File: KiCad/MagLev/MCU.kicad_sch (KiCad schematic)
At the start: 73 parts, among them J2 Programming header, J4 USB_B_Micro, Q1 ZX5T851GTA, Q16 TEMT7000X01, U6 ATmega328P-A, U8 FT232RL, U9 LM1117MP-5.0, Y3 J49SMH-16MHz

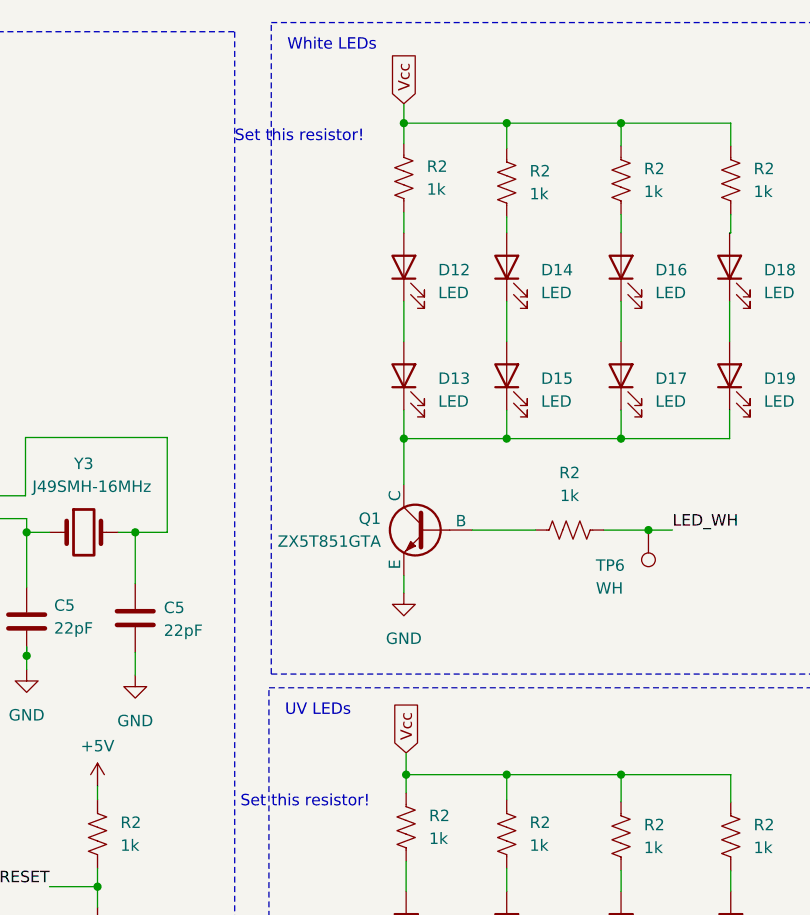
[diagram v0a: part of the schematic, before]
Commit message: Finish layout up to TPs.
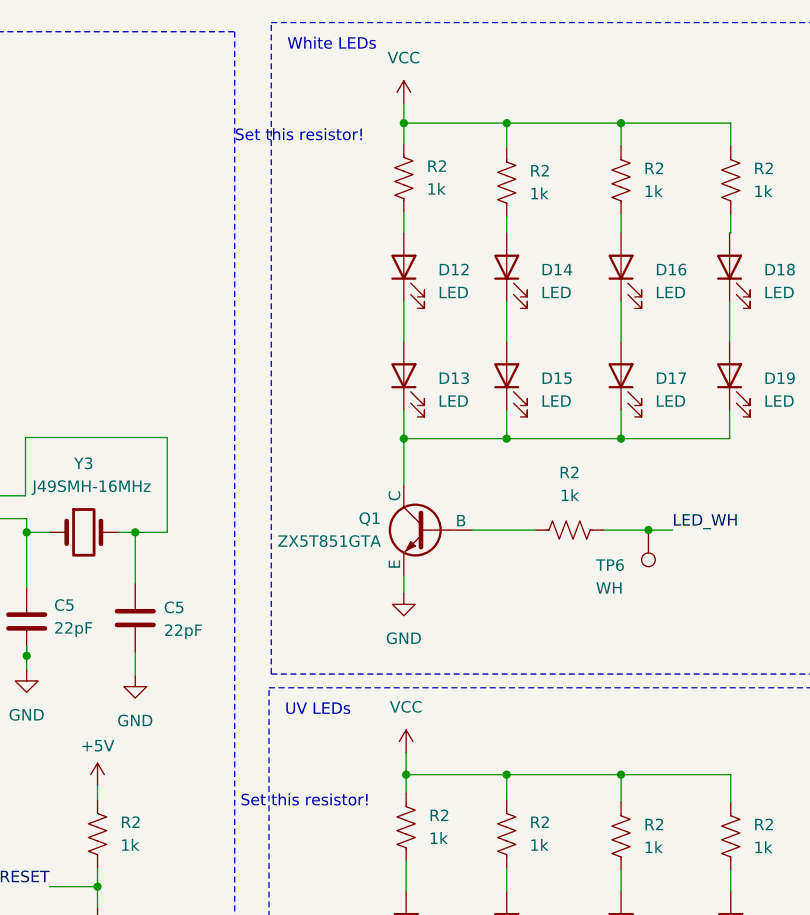
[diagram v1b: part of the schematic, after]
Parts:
- J4: footprint Connector_USB:USB_Micro-B_Amphenol_10118193-0001LF_Horizontal -> Connector_USB:USB_Micro-B_Amphenol_10104110_Horizontal
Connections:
- net Vcc is gone; now on net VCC: R2.2, R2.2, R2.2, R2.2, R2.2, R2.2, R2.2, R2.2
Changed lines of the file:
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@@
     (effects (font (size 1.27 1.27)) (justify left bottom))
-  )
-  (global_label "Vcc" (shape input) (at 235.458 25.527 90) (fields_autoplaced)
-    (effects (font (size 1.27 1.27)) (justify left))
-    (property "Intersheetrefs" "${INTERSHEET_REFS}" (at 235.458 19.276 90)
-      (effects (font (size 1.27 1.27)) (justify left) hide)
-    )
-  )
-  (global_label "Vcc" (shape input) (at 235.712 97.663 90) (fields_autoplaced)
-    (effects (font (size 1.27 1.27)) (justify left))
-    (property "Intersheetrefs" "${INTERSHEET_REFS}" (at 235.712 91.412 90)
-      (effects (font (size 1.27 1.27)) (justify left) hide)
-    )
   )
   (hierarchical_label "En_sig" (shape input) (at 178.816 102.108 0) (fields_autoplaced)
@@
     )
   )
+  (symbol (lib_id "power:VCC") (at 235.458 25.527 0) (unit 1)
+    (in_bom yes) (on_board yes) (dnp no) (fields_autoplaced)
+    (property "Reference" "#PWR048" (at 235.458 29.337 0)
+      (effects (font (size 1.27 1.27)) hide)
+    )
+    (property "Value" "VCC" (at 235.458 20.447 0)
+      (effects (font (size 1.27 1.27)))
+    )
+    (property "Footprint" "" (at 235.458 25.527 0)
+      (effects (font (size 1.27 1.27)) hide)
+    )
+    (property "Datasheet" "" (at 235.458 25.527 0)
+      (effects (font (size 1.27 1.27)) hide)
+    )
+    (pin "1")
+    (instances
+      (project "MagLev"
+        (path "/5eab7e8b-54e1-47d0-9dc3-1e7c3fa2f560"
+          (reference "#PWR048") (unit 1)
+        )
+        (path "/5eab7e8b-54e1-47d0-9dc3-1e7c3fa2f560/f228425d-6c39-40c9-8e00-a9ebad8217db"
+          (reference "#PWR048") (unit 1)
+        )
+      )
+    )
+  )
   (symbol (lib_id "Device:LED") (at 235.458 55.753 90) (unit 1)
     (in_bom yes) (on_board yes) (dnp no) (fields_autoplaced)
@@
       (effects (font (size 1.27 1.27)))
     )
-    (property "Footprint" "Connector_USB:USB_Micro-B_Amphenol_10118193-0001LF_Horizontal" (at 33.147 85.598 0)
+    (property "Footprint" "Connector_USB:USB_Micro-B_Amphenol_10104110_Horizontal" (at 33.147 85.598 0)
       (effects (font (size 1.27 1.27)) hide)
     )
@@
         )
       )
+    )
+  )
+  (symbol (lib_id "power:VCC") (at 235.712 97.663 0) (unit 1)
+    (in_bom yes) (on_board yes) (dnp no) (fields_autoplaced)
+    (property "Reference" "#PWR048" (at 235.712 101.473 0)
+      (effects (font (size 1.27 1.27)) hide)
+    )
+    (property "Value" "VCC" (at 235.712 92.583 0)
+      (effects (font (size 1.27 1.27)))
+    )
+    (property "Footprint" "" (at 235.712 97.663 0)
+      (effects (font (size 1.27 1.27)) hide)
+    )
+    (property "Datasheet" "" (at 235.712 97.663 0)
+      (effects (font (size 1.27 1.27)) hide)
+    )
+    (pin "1")
+    (instances
+      (project "MagLev"
+        (path "/5eab7e8b-54e1-47d0-9dc3-1e7c3fa2f560"
+          (reference "#PWR048") (unit 1)
+        )
+        (path "/5eab7e8b-54e1-47d0-9dc3-1e7c3fa2f560/f228425d-6c39-40c9-8e00-a9ebad8217db"
+          (reference "#PWR053") (unit 1)
+        )
+      )

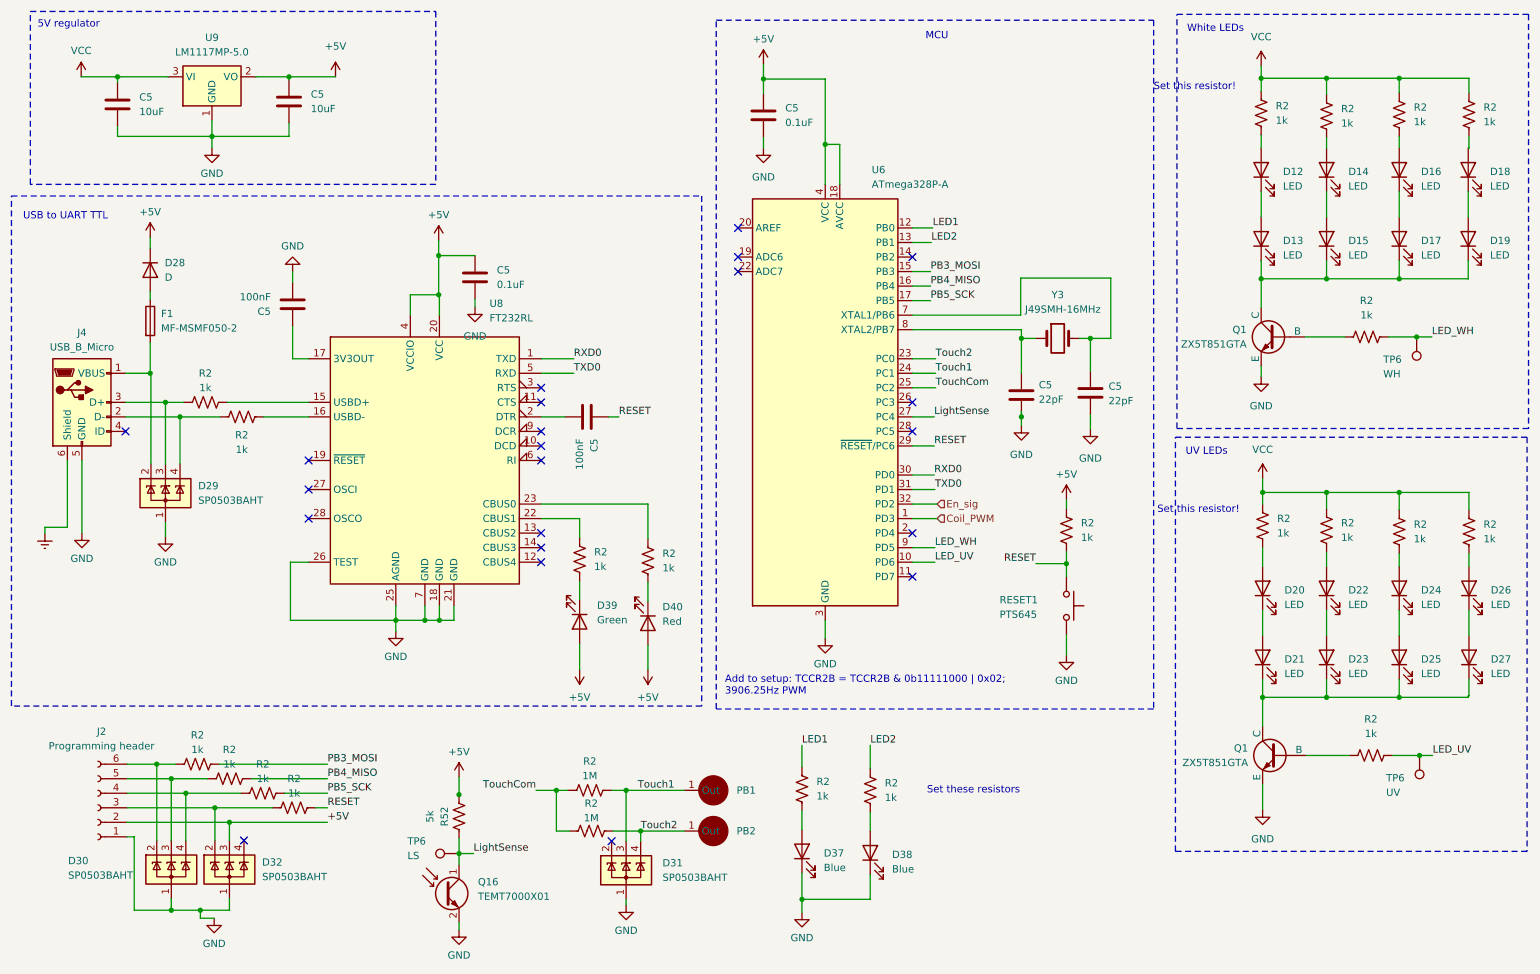
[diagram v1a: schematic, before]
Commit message: Route TPs, increase power trace size.
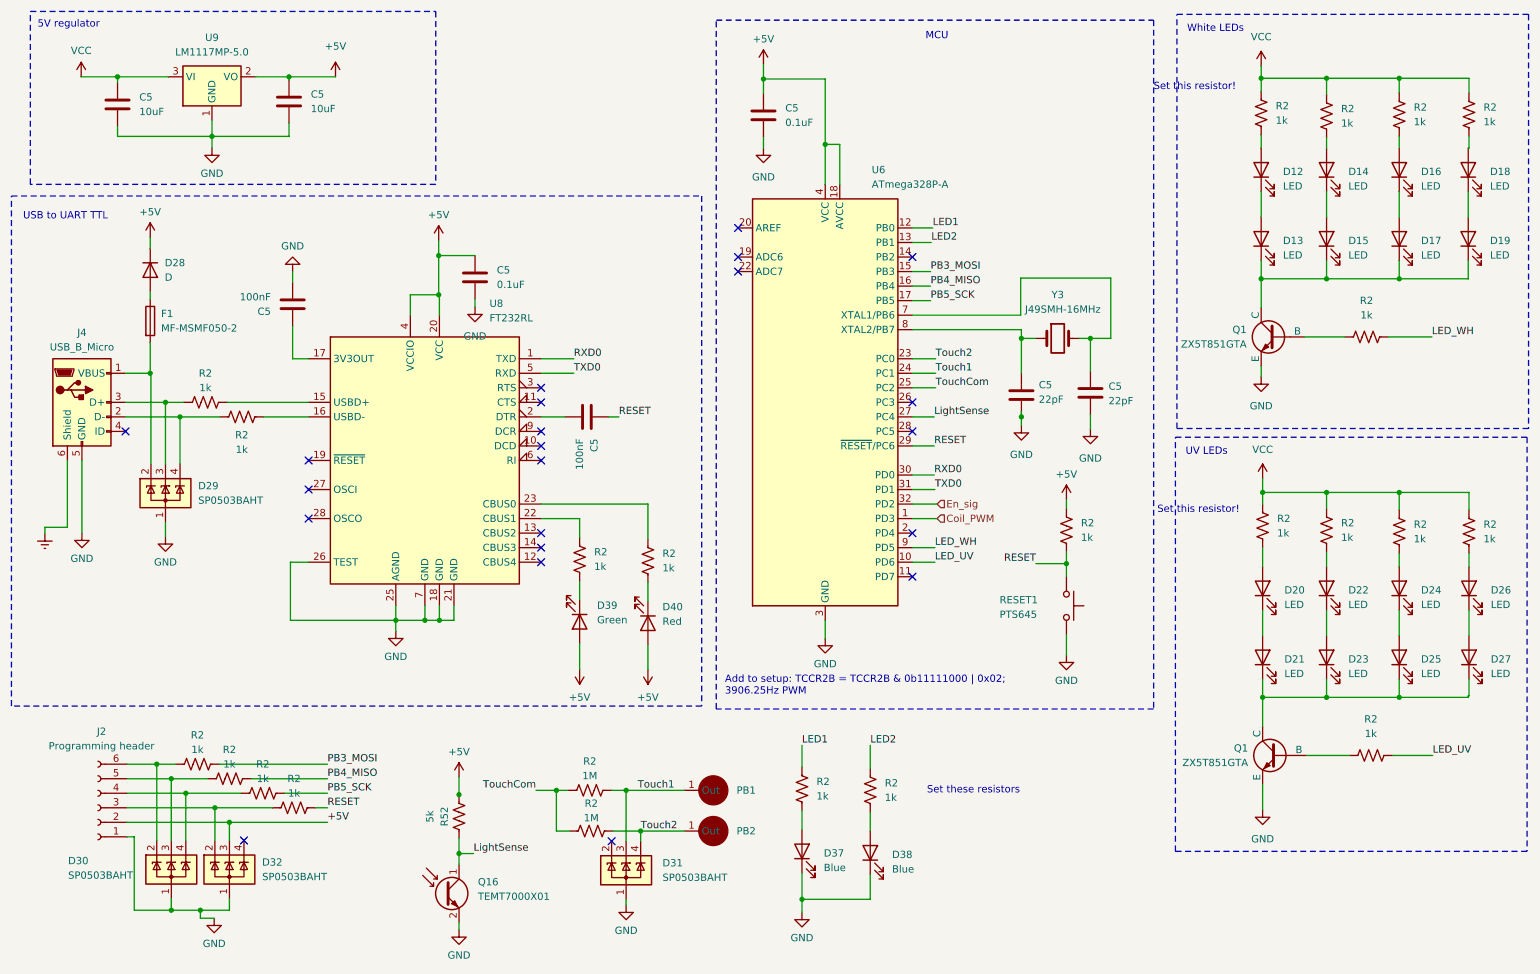
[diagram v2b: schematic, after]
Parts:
- removed TP6: LS, TestPoint:TestPoint_Pad_D2.0mm, symbol Connector:TestPoint
- removed TP6: WH, TestPoint:TestPoint_Pad_D2.0mm, symbol Connector:TestPoint
- removed TP6: UV, TestPoint:TestPoint_Pad_D2.0mm, symbol Connector:TestPoint
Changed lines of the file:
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@@
   (junction (at 235.712 100.076) (diameter 0) (color 0 0 0 0)
   )
-  (junction (at 263.144 146.05) (diameter 0) (color 0 0 0 0)
-  )
   (junction (at 41.275 79.248) (diameter 0) (color 0 0 0 0)
   )
@@
   )
   (junction (at 201.422 112.522) (diameter 0) (color 0 0 0 0)
-  )
-  (junction (at 262.636 72.898) (diameter 0) (color 0 0 0 0)
   )
   (junction (at 35.56 27.432) (diameter 0) (color 0 0 0 0)
@@
     (stroke (width 0) (type default))
   )
-  (wire (pts (xy 263.144 146.05) (xy 265.43 146.05))
+  (wire (pts (xy 258.445 146.05) (xy 265.43 146.05))
     (stroke (width 0) (type default))
   )
@@
     (stroke (width 0) (type default))
   )
-  (wire (pts (xy 257.683 72.898) (xy 262.636 72.898))
+  (wire (pts (xy 257.683 72.898) (xy 265.303 72.898))
     (stroke (width 0) (type default))
   )
@@
     (stroke (width 0) (type default))
   )
-  (wire (pts (xy 258.445 146.05) (xy 263.144 146.05))
-    (stroke (width 0) (type default))
-  )
   (wire (pts (xy 174.498 56.388) (xy 177.8 56.388))
     (stroke (width 0) (type default))
@@
   )
   (wire (pts (xy 65.786 112.268) (xy 65.786 122.428))
-    (stroke (width 0) (type default))
-  )
-  (wire (pts (xy 262.636 72.898) (xy 265.303 72.898))
     (stroke (width 0) (type default))
   )
@@
         (path "/5eab7e8b-54e1-47d0-9dc3-1e7c3fa2f560/f228425d-6c39-40c9-8e00-a9ebad8217db"
           (reference "#PWR051") (unit 1)
-        )
-      )
-    )
-  )
-  (symbol (lib_id "Connector:TestPoint") (at 95.25 163.195 90) (unit 1)
-    (in_bom yes) (on_board yes) (dnp no)
-    (property "Reference" "TP6" (at 86.233 161.036 90)
-      (effects (font (size 1.27 1.27)) (justify right))
-    )
-    (property "Value" "LS" (at 86.233 163.576 90)
-      (effects (font (size 1.27 1.27)) (justify right))
-    )
-    (property "Footprint" "TestPoint:TestPoint_Pad_D2.0mm" (at 95.25 158.115 0)
-      (effects (font (size 1.27 1.27)) hide)
-    )
-    (property "Datasheet" "~" (at 95.25 158.115 0)
-      (effects (font (size 1.27 1.27)) hide)
-    )
-    (pin "1")
-    (instances
-      (project "MagLev"
-        (path "/5eab7e8b-54e1-47d0-9dc3-1e7c3fa2f560"
-          (reference "TP6") (unit 1)
-        )
-        (path "/5eab7e8b-54e1-47d0-9dc3-1e7c3fa2f560/f228425d-6c39-40c9-8e00-a9ebad8217db"
-          (reference "TP17") (unit 1)
         )
       )
@@
     )
   )
-  (symbol (lib_id "Connector:TestPoint") (at 262.636 72.898 180) (unit 1)
-    (in_bom yes) (on_board yes) (dnp no)
-    (property "Reference" "TP6" (at 256.794 76.835 0)
-      (effects (font (size 1.27 1.27)) (justify right))
-    )
-    (property "Value" "WH" (at 256.794 79.375 0)
-      (effects (font (size 1.27 1.27)) (justify right))
-    )
-    (property "Footprint" "TestPoint:TestPoint_Pad_D2.0mm" (at 257.556 72.898 0)
-      (effects (font (size 1.27 1.27)) hide)
-    )
-    (property "Datasheet" "~" (at 257.556 72.898 0)
-      (effects (font (size 1.27 1.27)) hide)
-    )
-    (pin "1")
-    (instances
-      (project "MagLev"
-        (path "/5eab7e8b-54e1-47d0-9dc3-1e7c3fa2f560"
-          (reference "TP6") (unit 1)
-        )
-        (path "/5eab7e8b-54e1-47d0-9dc3-1e7c3fa2f560/f228425d-6c39-40c9-8e00-a9ebad8217db"
-          (reference "TP19") (unit 1)
-        )
-      )
-    )
-  )
   (symbol (lib_id "Power_Protection:SP0503BAHT") (at 55.118 165.989 0) (unit 1)
     (in_bom yes) (on_board yes) (dnp no) (fields_autoplaced)
@@
         )
       )
-    )
-  )
-  (symbol (lib_id "Connector:TestPoint") (at 263.144 146.05 180) (unit 1)
-    (in_bom yes) (on_board yes) (dnp no)
-    (property "Reference" "TP6" (at 257.302 149.987 0)
-      (effects (font (size 1.27 1.27)) (justify right))
-    )
-    (property "Value" "UV" (at 257.302 152.527 0)
-      (effects (font (size 1.27 1.27)) (justify right))
-    )
-    (property "Footprint" "TestPoint:TestPoint_Pad_D2.0mm" (at 258.064 146.05 0)
-      (effects (font (size 1.27 1.27)) hide)
-    )
-    (property "Datasheet" "~" (at 258.064 146.05 0)
-      (effects (font (size 1.27 1.27)) hide)
-    )
-    (pin "1")
-    (instances
-      (project "MagLev"
-        (path "/5eab7e8b-54e1-47d0-9dc3-1e7c3fa2f560"
-          (reference "TP6") (unit 1)
-        )
-        (path "/5eab7e8b-54e1-47d0-9dc3-1e7c3fa2f560/f228425d-6c39-40c9-8e00-a9ebad8217db"
-          (reference "TP18") (unit 1)
-        )
-      )

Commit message: Fix DRC errors.
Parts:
- J4: footprint Connector_USB:USB_Micro-B_Amphenol_10104110_Horizontal -> Maglev_Footprint_Library:USB_Micro-B_Amphenol_10104110_Horizontal_Overhang
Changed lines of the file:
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@@
       (effects (font (size 1.27 1.27)))
     )
-    (property "Footprint" "Connector_USB:USB_Micro-B_Amphenol_10104110_Horizontal" (at 33.147 85.598 0)
+    (property "Footprint" "Maglev_Footprint_Library:USB_Micro-B_Amphenol_10104110_Horizontal_Overhang" (at 33.147 85.598 0)
       (effects (font (size 1.27 1.27)) hide)
     )
